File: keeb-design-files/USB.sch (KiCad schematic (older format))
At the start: 38 parts, among them J3 USB_B, J4 S2B-PH-K-S, J5 Conn_01x02, SW71 SW_SPDT, U3 USBLC6-2SC6, U4 BQ24075, U5 NXE2S0505MC, U6 STC3100, U7 LD39050P

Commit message: More placement before layout
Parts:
- FB1: value 100 @ 100MHz -> 60 @ 100MHz; LCSC Part Number (none) -> C76816
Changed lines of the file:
@@
 P 1900 1300
 F 0 "FB1" V 1626 1300 50  0000 C CNN
-F 1 "100 @ 100MHz" V 1717 1300 50  0000 C CNN
+F 1 "60 @ 100MHz" V 1717 1300 50  0000 C CNN
 F 2 "Resistor_SMD:R_0603_1608Metric_Pad1.05x0.95mm_HandSolder" V 1830 1300 50  0001 C CNN
 F 3 "~" H 1900 1300 50  0001 C CNN
+F 4 "C76816" H 1900 1300 50  0001 C CNN "LCSC Part Number"
 	1    1900 1300
 	0    1    1    0

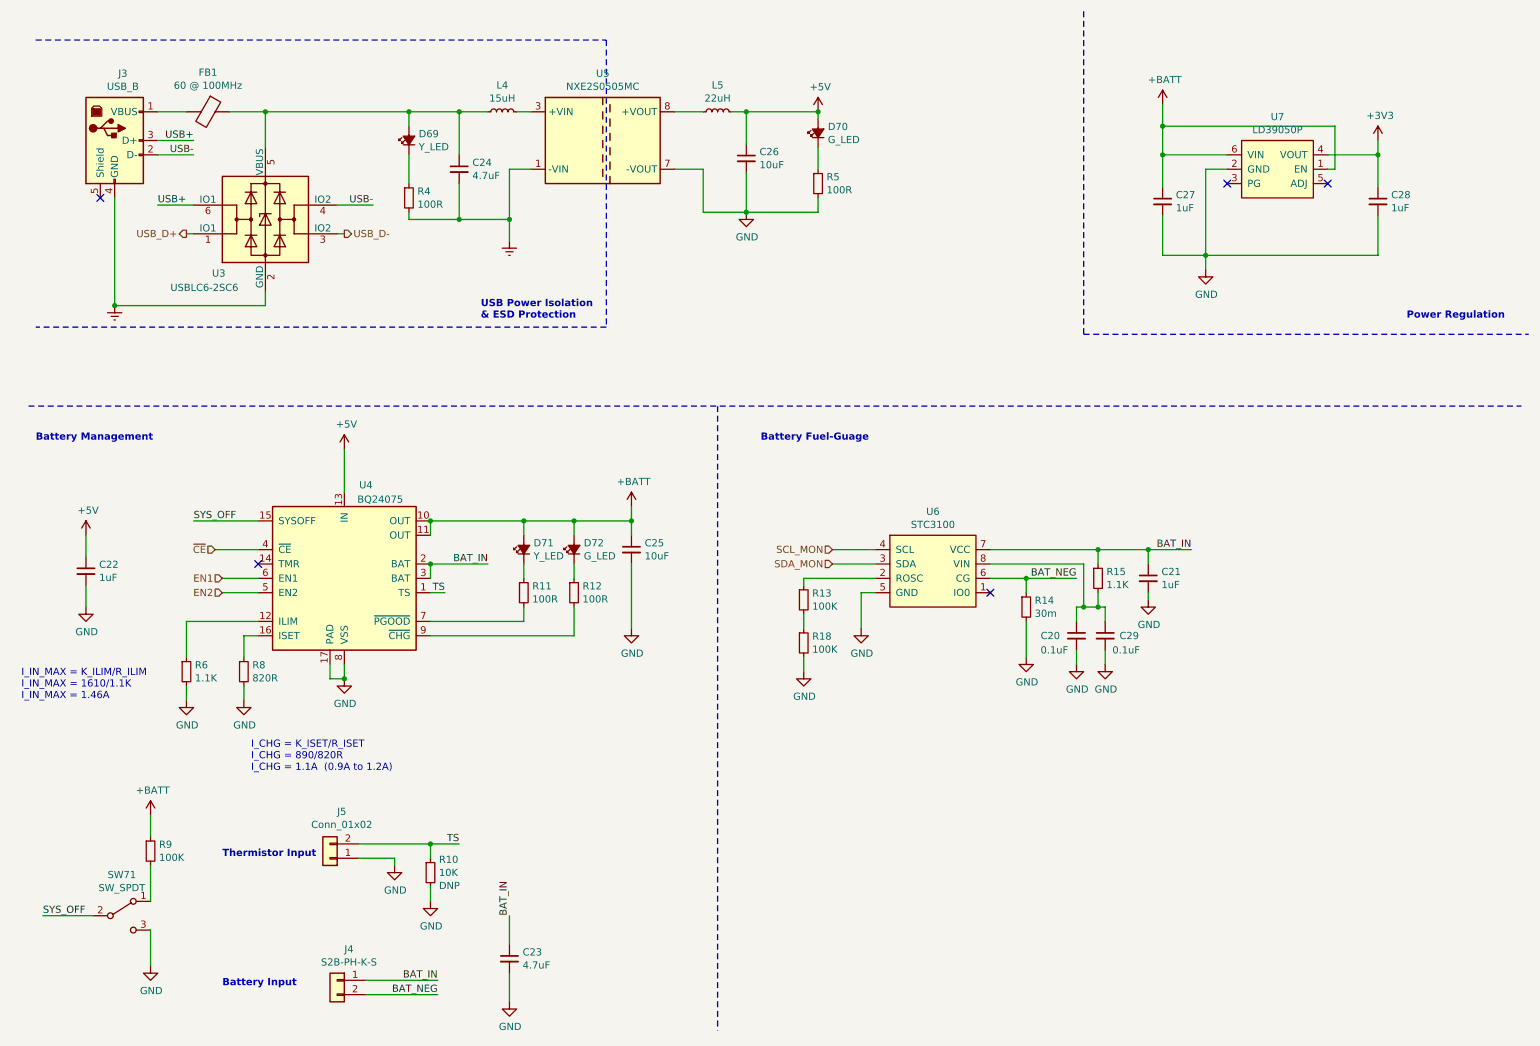
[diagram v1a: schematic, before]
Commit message: Re-map MCU pins, Add LEDs, Remove USB Isolation cause it couldn't handle the POWER! More routing done
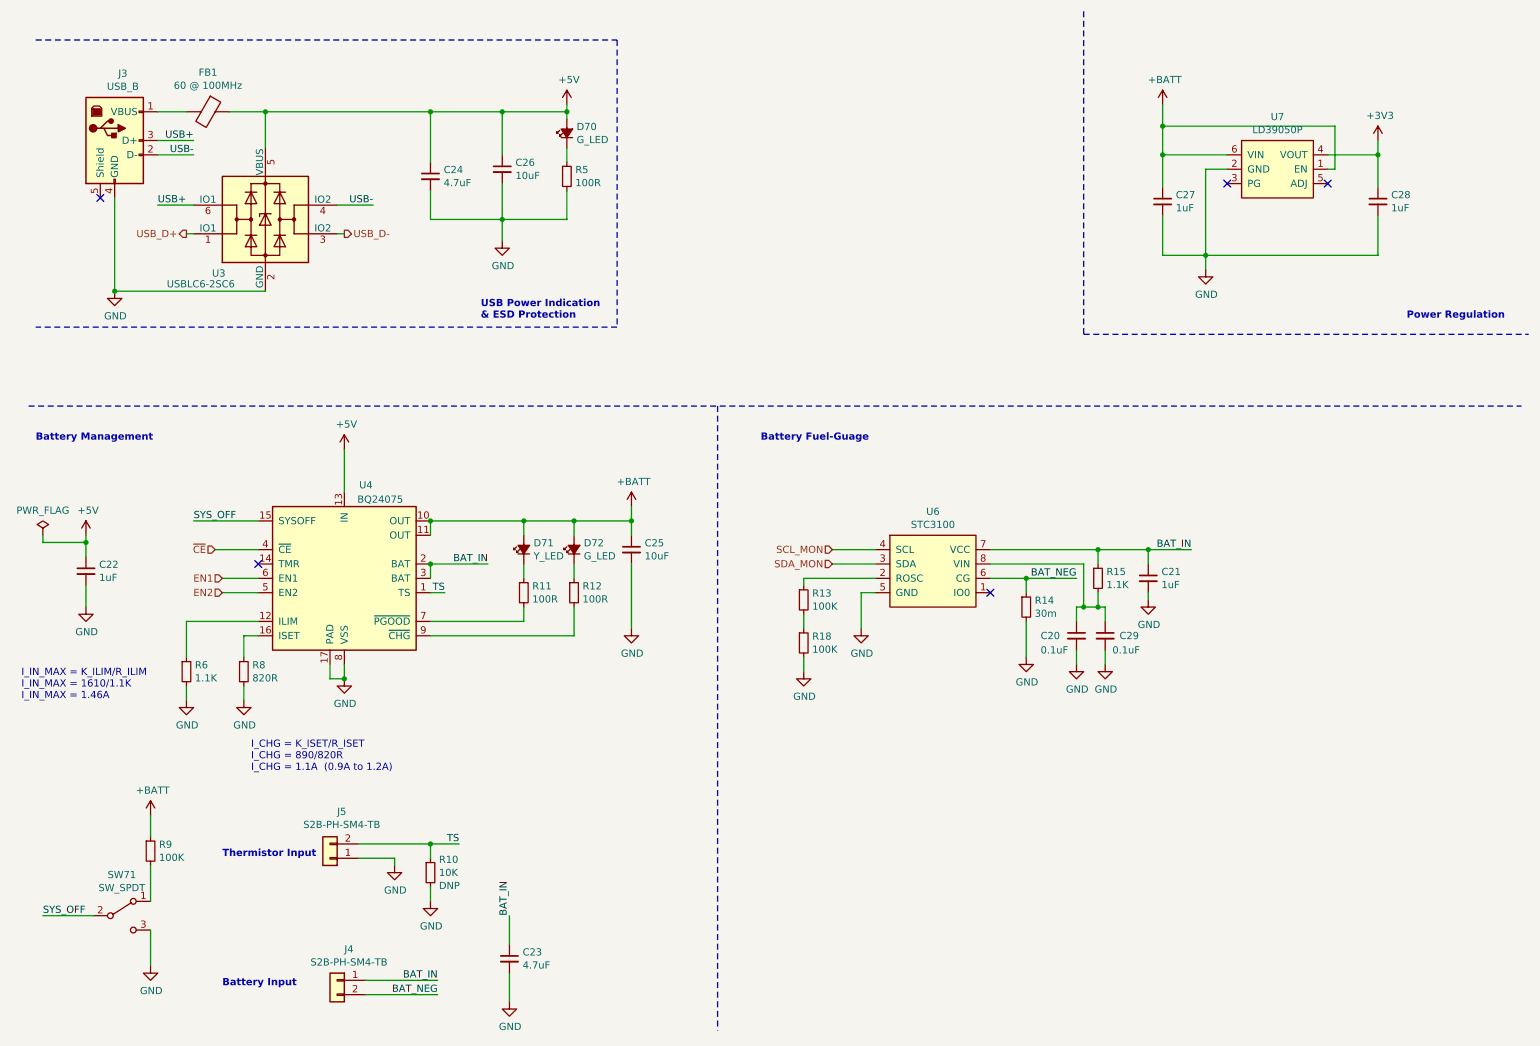
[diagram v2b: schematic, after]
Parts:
- removed D69: Y_LED, LED_SMD:LED_0603_1608Metric, symbol Device:LED_Small_ALT
- removed L4: 15uH, Inductor_SMD:L_Bourns_SRR1260, symbol Device:L_Small
- removed L5: 22uH, Inductor_SMD:L_Bourns_SRR1260, symbol Device:L_Small
- removed R4: 100R, Resistor_SMD:R_0402_1005Metric, symbol Device:R_Small
- removed U5: NXE2S0505MC, Converter_DCDC:Converter_DCDC_muRata_NXE2SxxxxMC_THT, symbol Regulator_Switching:NXE2S0505MC
- J4: value S2B-PH-K-S -> S2B-PH-SM4-TB; footprint Connector_JST:JST_PH_S2B-PH-K_1x02_P2.00mm_Horizontal -> lib_fp:JST_PH_S2B-PH-SM4-TB_1x02-1MP_P2.00mm_Horizontal
- J5: value Conn_01x02 -> S2B-PH-SM4-TB; footprint Connector_JST:JST_PH_S2B-PH-K_1x02_P2.00mm_Horizontal -> lib_fp:JST_PH_S2B-PH-SM4-TB_1x02-1MP_P2.00mm_Horizontal
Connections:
- net Earth is gone; now on net GND: C24.2, J3.4 (GND), U3.2 (GND)
- net +5V: now also C24.1, FB1.1, U3.5 (VBUS)
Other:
- note added: "USB Power Indication\n& ESD Protection"
- note removed: "USB Power Isolation\n& ESD Protection"
- moved on the sheet: C24, C26, D70, R5

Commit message: Create gerbers picknplace and bom
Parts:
- R11, R12, R5: LCSC Part Number C25741 -> C25076
- R15, R6: value 1.1K -> 1.2K; LCSC Part Number C25860 -> C25862
- R8: value 820R -> 1K; LCSC Part Number C25135 -> C25726
- U6: LCSC Part Number (none) -> C155587
- U7: LCSC Part Number (none) -> C132827
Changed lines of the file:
@@
 F 2 "Resistor_SMD:R_0402_1005Metric" H 4400 1750 50  0001 C CNN
 F 3 "~" H 4400 1750 50  0001 C CNN
-F 4 "C25741" H 4400 1750 50  0001 C CNN "LCSC Part Number"
+F 4 "C25076" H 4400 1750 50  0001 C CNN "LCSC Part Number"
 	1    4400 1750
 	1    0    0    -1
@@
 P 2150 5200
 F 0 "R8" H 2209 5246 50  0000 L CNN
-F 1 "820R" H 2209 5155 50  0000 L CNN
+F 1 "1K" H 2209 5155 50  0000 L CNN
 F 2 "Resistor_SMD:R_0402_1005Metric" H 2150 5200 50  0001 C CNN
 F 3 "~" H 2150 5200 50  0001 C CNN
-F 4 "C25135" H 2209 5109 50  0001 L CNN "LCSC Part Number"
+F 4 "C25726" H 2209 5109 50  0001 L CNN "LCSC Part Number"
 	1    2150 5200
 	1    0    0    -1
@@
 P 1750 5200
 F 0 "R6" H 1809 5246 50  0000 L CNN
-F 1 "1.1K" H 1809 5155 50  0000 L CNN
+F 1 "1.2K" H 1809 5155 50  0000 L CNN
 F 2 "Resistor_SMD:R_0402_1005Metric" H 1750 5200 50  0001 C CNN
 F 3 "~" H 1750 5200 50  0001 C CNN
-F 4 "C25860" H 1750 5200 50  0001 C CNN "LCSC Part Number"
+F 4 "C25862" H 1750 5200 50  0001 C CNN "LCSC Part Number"
 	1    1750 5200
 	1    0    0    -1
@@
 F 2 "Resistor_SMD:R_0402_1005Metric" H 4100 4650 50  0001 C CNN
 F 3 "~" H 4100 4650 50  0001 C CNN
-F 4 "C25741" H 4100 4650 50  0001 C CNN "LCSC Part Number"
+F 4 "C25076" H 4100 4650 50  0001 C CNN "LCSC Part Number"
 	1    4100 4650
 	1    0    0    -1
@@
 F 2 "Resistor_SMD:R_0402_1005Metric" H 4450 4650 50  0001 C CNN
 F 3 "~" H 4450 4650 50  0001 C CNN
-F 4 "C25741" H 4450 4650 50  0001 C CNN "LCSC Part Number"
+F 4 "C25076" H 4450 4650 50  0001 C CNN "LCSC Part Number"
 	1    4450 4650
 	1    0    0    -1
@@
 P 8100 4550
 F 0 "R15" H 8159 4596 50  0000 L CNN
-F 1 "1.1K" H 8159 4505 50  0000 L CNN
+F 1 "1.2K" H 8159 4505 50  0000 L CNN
 F 2 "Resistor_SMD:R_0402_1005Metric" H 8100 4550 50  0001 C CNN
 F 3 "~" H 8100 4550 50  0001 C CNN
-F 4 "C25860" H 8100 4550 50  0001 C CNN "LCSC Part Number"
+F 4 "C25862" H 8100 4550 50  0001 C CNN "LCSC Part Number"
 	1    8100 4550
 	1    0    0    -1
@@
 F 2 "Package_DFN_QFN:DFN-6-1EP_3x3mm_P0.95mm_EP1.7x2.6mm" H 9350 1250 50  0001 C CNN
 F 3 "https://datasheet.lcsc.com/szlcsc/STMicroelectronics-LD39050PU33R_C132827.pdf" H 9350 1550 50  0001 C CNN
+F 4 "C132827" H 9350 1700 50  0001 C CNN "LCSC Part Number"
 	1    9350 1700
 	1    0    0    -1
@@
 F 2 "Package_DFN_QFN:DFN-8-1EP_3x3mm_P0.5mm_EP1.66x2.38mm" H 6950 4500 50  0001 C CNN
 F 3 "" H 6950 4500 50  0001 C CNN
+F 4 "C155587" H 6950 4500 50  0001 C CNN "LCSC Part Number"
 	1    6950 4500
 	1    0    0    -1

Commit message: Re-Generate Gerbers
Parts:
- R8: LCSC Part Number C25726 -> C11702
- U7: footprint Package_DFN_QFN:DFN-6-1EP_3x3mm_P0.95mm_EP1.7x2.6mm -> lib_fp:DFN-6-1EP_3x3mm_P0.95mm_EP1.7x2.6mm
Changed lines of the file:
@@
 F 2 "Resistor_SMD:R_0402_1005Metric" H 2150 5200 50  0001 C CNN
 F 3 "~" H 2150 5200 50  0001 C CNN
-F 4 "C25726" H 2209 5109 50  0001 L CNN "LCSC Part Number"
+F 4 "C11702" H 2209 5109 50  0001 L CNN "LCSC Part Number"
 	1    2150 5200
 	1    0    0    -1
@@
 F 0 "U7" H 9350 2065 50  0000 C CNN
 F 1 "LD39050P" H 9350 1974 50  0000 C CNN
-F 2 "Package_DFN_QFN:DFN-6-1EP_3x3mm_P0.95mm_EP1.7x2.6mm" H 9350 1250 50  0001 C CNN
+F 2 "lib_fp:DFN-6-1EP_3x3mm_P0.95mm_EP1.7x2.6mm" H 9350 1250 50  0001 C CNN
 F 3 "https://datasheet.lcsc.com/szlcsc/STMicroelectronics-LD39050PU33R_C132827.pdf" H 9350 1550 50  0001 C CNN
 F 4 "C132827" H 9350 1700 50  0001 C CNN "LCSC Part Number"
